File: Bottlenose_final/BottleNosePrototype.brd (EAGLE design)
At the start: 100 x 80 mm, 22 parts, among them Q1 16MHz, U1 MCP73831, X2 USBSMD

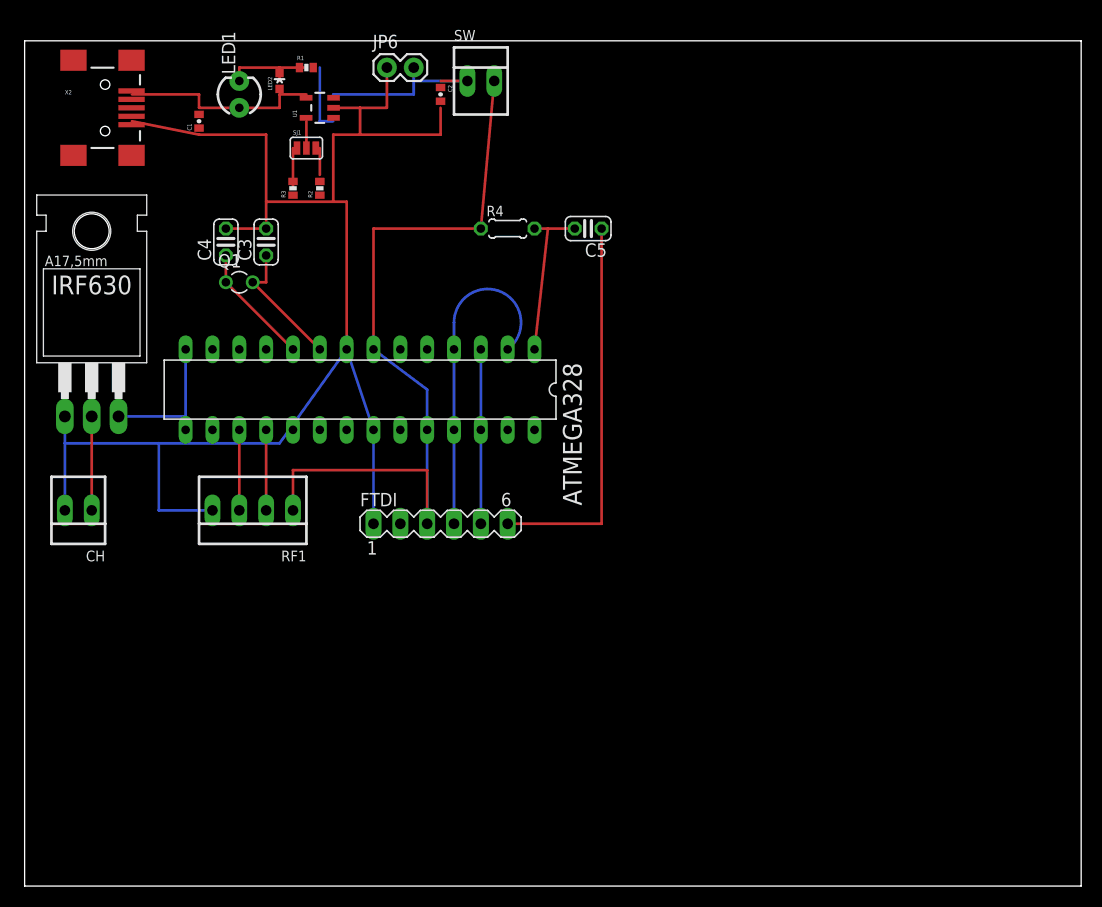
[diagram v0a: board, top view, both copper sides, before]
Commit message: I have added dimensions to the .brd file.
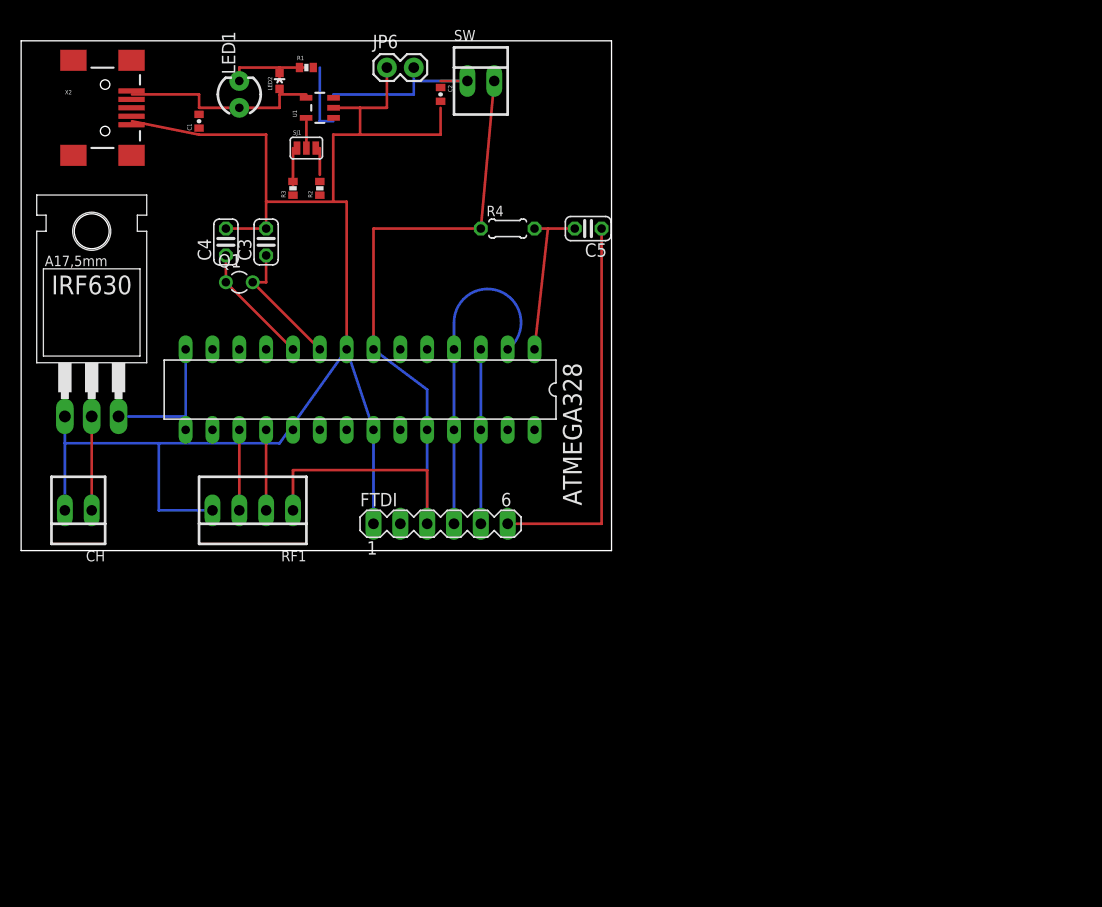
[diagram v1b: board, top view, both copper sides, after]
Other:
- board size 100 x 80 mm -> 55.9 x 48.2 mm
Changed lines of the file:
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@@
 <board>
 <plain>
-<wire x1="0" y1="0" x2="100" y2="0" width="0" layer="20"/>
-<wire x1="100" y1="0" x2="100" y2="80" width="0" layer="20"/>
-<wire x1="100" y1="80" x2="0" y2="80" width="0" layer="20"/>
-<wire x1="0" y1="80" x2="0" y2="0" width="0" layer="20"/>
+<wire x1="-0.33" y1="31.75" x2="55.55" y2="31.75" width="0" layer="20"/>
+<wire x1="55.55" y1="31.75" x2="55.55" y2="80" width="0" layer="20"/>
+<wire x1="55.55" y1="80" x2="-0.33" y2="80" width="0" layer="20"/>
+<dimension x1="55.88" y1="29.21" x2="0" y2="29.21" x3="27.94" y3="25.4" layer="1"/>
+<dimension x1="59.69" y1="31.75" x2="59.69" y2="80.01" x3="64.77" y3="55.88" layer="1"/>
+<wire x1="-0.33" y1="31.75" x2="-0.33" y2="80" width="0" layer="20"/>
 </plain>
 <attributes>

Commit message: There was a value error on a couple of connections
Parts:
- FTDI: value (none) -> FTDI
- SJ1: value (none) -> SJ1
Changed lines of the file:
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@@
 <element name="C2" library="SparkFun" package="0402-CAP" value="4.7uF" x="39.37" y="74.93" rot="R270"/>
 <element name="R2" library="SparkFun" package="0402-RES" value="2k" x="27.94" y="66.04" rot="R90"/>
-<element name="SJ1" library="SparkFun" package="SJ_3" value="" x="26.67" y="69.85"/>
+<element name="SJ1" library="SparkFun" package="SJ_3" value="SJ1" x="26.67" y="69.85"/>
 <element name="R3" library="SparkFun" package="0402-RES" value="10k" x="25.4" y="66.04" rot="R90"/>
 <element name="LED1" library="SparkFun" package="LED3MM" value="DNP" x="20.32" y="74.93" rot="R90"/>
@@
 <element name="C3" library="rcl" package="C025-024X044" value="22pF" x="22.86" y="60.96" rot="R90"/>
 <element name="C4" library="rcl" package="C025-024X044" value="22pF" x="19.05" y="60.96" rot="R90"/>
-<element name="FTDI" library="con-lstb" package="MA06-1" value="" x="39.37" y="34.29">
+<element name="FTDI" library="con-lstb" package="MA06-1" value="FTDI" x="39.37" y="34.29">
 <attribute name="OC_NEWARK" value="unknown" x="60.96" y="-25.4" size="1.778" layer="27" display="off"/>
 <attribute name="MPN" value="" x="60.96" y="-25.4" size="1.778" layer="27" display="off"/>
